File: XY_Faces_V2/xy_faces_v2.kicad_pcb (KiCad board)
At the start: 4 copper layers, 83 x 98 mm, 32 parts, among them J1 CON-5040500591, J2 Conn_01x01, J3 Conn_01x01, J4 Conn_01x01, J5 Conn_01x01, U1 VEML7700, U2 MCP9808_DFN, U3 DRV2605LDGS

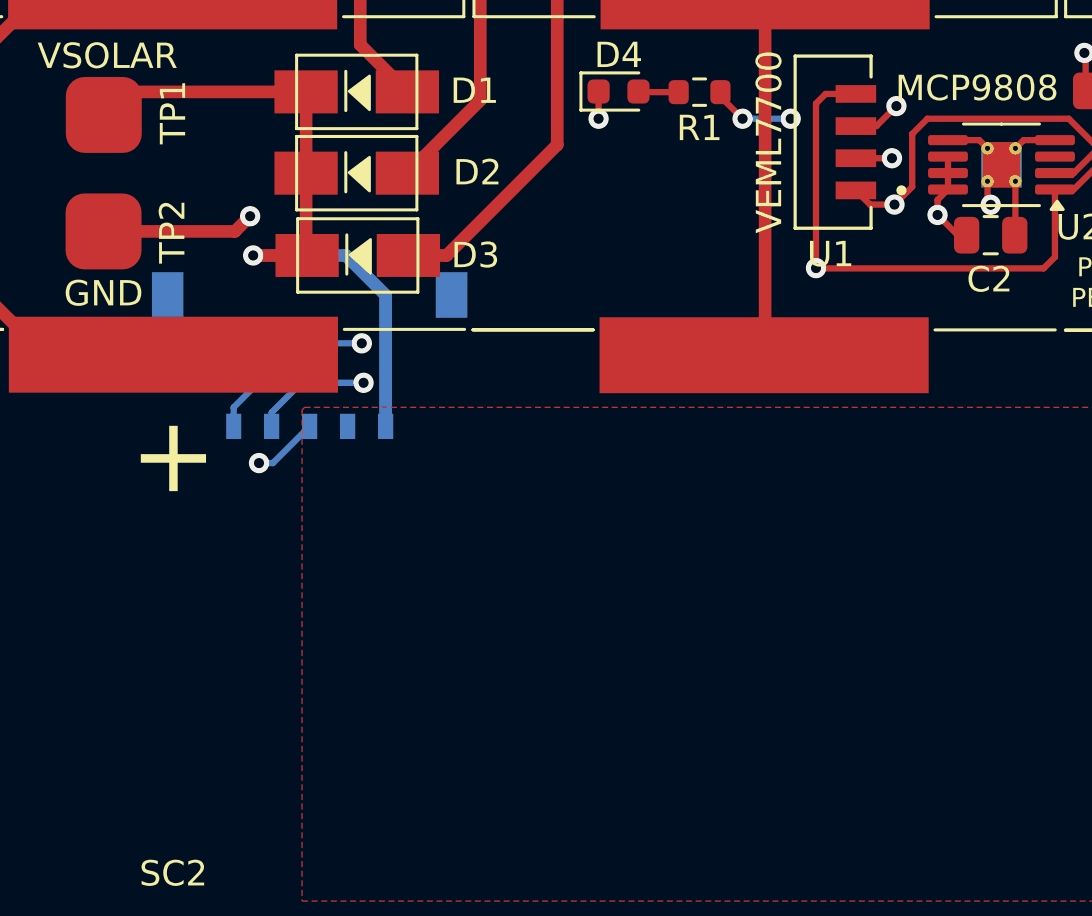
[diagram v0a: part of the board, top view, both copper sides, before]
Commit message: Updated Boards with DF13 Connectors
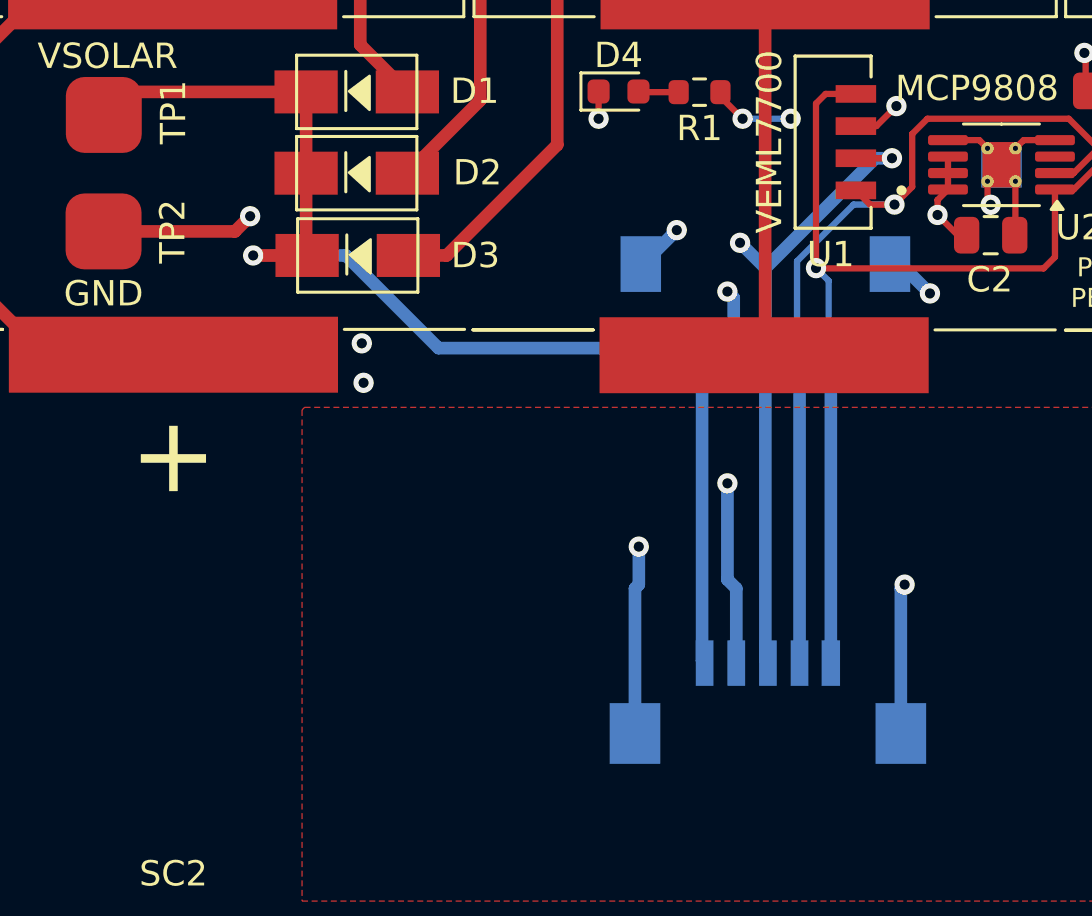
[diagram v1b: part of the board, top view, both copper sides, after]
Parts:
- removed J1: CON-5040500591, SolarPanelBoards:CON_5040500591
- added CN1: DF13A-5P-1.25H(21), easyeda2kicad:CONN-SMD_5P-P1.25_HRS_DF13A-5P-1.25H, B.Cu at (144.5, 120.0)
- added CN2: DF13C-5P-1.25V(21), easyeda2kicad:CONN-SMD_DF13C-5P-1.25V-21, B.Cu at (144.6, 136.0)
- moved G*** 19.5 mm to (126.1, 95.4)
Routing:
- net GND: track 41.7 -> 68.7 mm, vias 10 -> 16
- net +3V3: track 45.2 -> 66.5 mm
- net VSOLAR: track 28.0 -> 48.7 mm
- net SCL: track 45.7 -> 61.7 mm
- net SDA: track 50.0 -> 59.0 mm
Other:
- board text added: "The PROVES Kit V3"
- board text removed: "The PROVES Kit V1.5"

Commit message: Production Files for V2 XY Boards
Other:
- board text added: "PROVES XY SOLAR: KIT V3 AMANDA EWING, NICOLE MAGGARD, Michael Pham"
- board text removed: "PROVES XY SOLAR: YEARLING KIT V1.5 AMANDA EWING, NICOLE MAGGARD"
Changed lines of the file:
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@@
 		)
 	)
-	(gr_text "PROVES XY SOLAR: YEARLING KIT V1.5\nAMANDA EWING, NICOLE MAGGARD"
+	(gr_text "PROVES XY SOLAR: KIT V3\nAMANDA EWING, NICOLE MAGGARD, Michael Pham"
 		(at 112.29 68.36 0)
 		(layer "B.SilkS")
